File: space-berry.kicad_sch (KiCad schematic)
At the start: 0 parts

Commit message: Stuff
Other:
- sheet PS_PWR renamed ZYNQ_PWR
- sheet PWR_template renamed PWR_3V3
- sheet PWR_template1 renamed PWR_3V3_AUX
- sheet PWR_template2 renamed PWR_1V8
- sheet PWR_template3 renamed PWR_1V2
- sheet PWR_template4 renamed PWR_0V85
- sheet PWR_template5 renamed PWR_5V0
- added sheet PS_DDR_MIO0-53 (PS_DDR_MIO0-53.kicad_sch)
- sheet PWR_0V85: file PWR_template.kicad_sch -> PWR_0V85.kicad_sch
- sheet PWR_1V2: file PWR_template.kicad_sch -> PWR_1V2.kicad_sch
- sheet PWR_1V8: file PWR_template.kicad_sch -> PWR_1V8.kicad_sch
- sheet PWR_3V3: file PWR_template.kicad_sch -> PWR_3V3.kicad_sch
- sheet PWR_3V3_AUX: file PWR_template.kicad_sch -> PWR_3V3_AUX.kicad_sch
- sheet PWR_5V0: file PWR_template.kicad_sch -> PWR_5V0.kicad_sch
- sheet ZYNQ_PWR: file PS_PWR.kicad_sch -> ZYNQ_PWR.kicad_sch
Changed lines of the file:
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@@
     (stroke (width 0.1524) (type solid))
     (fill (color 0 0 0 0.0000))
-    (property "Sheetname" "PS_PWR" (at 76.2 88.1884 0)
+    (property "Sheetname" "ZYNQ_PWR" (at 76.2 88.1884 0)
       (effects (font (size 1.27 1.27)) (justify left bottom))
     )
-    (property "Sheetfile" "PS_PWR.kicad_sch" (at 76.2 102.1846 0)
+    (property "Sheetfile" "ZYNQ_PWR.kicad_sch" (at 76.2 102.1846 0)
       (effects (font (size 1.27 1.27)) (justify left top))
     )
@@
     (stroke (width 0.1524) (type solid))
     (fill (color 0 0 0 0.0000))
-    (property "Sheetname" "PWR_template" (at 38.1 37.3884 0)
+    (property "Sheetname" "PWR_3V3" (at 38.1 37.3884 0)
       (effects (font (size 1.27 1.27)) (justify left bottom))
     )
-    (property "Sheetfile" "PWR_template.kicad_sch" (at 38.1 51.3846 0)
+    (property "Sheetfile" "PWR_3V3.kicad_sch" (at 38.1 51.3846 0)
       (effects (font (size 1.27 1.27)) (justify left top))
     )
@@
     (stroke (width 0.1524) (type solid))
     (fill (color 0 0 0 0.0000))
-    (property "Sheetname" "PWR_template3" (at 38.1 113.5884 0)
+    (property "Sheetname" "PWR_1V2" (at 38.1 113.5884 0)
       (effects (font (size 1.27 1.27)) (justify left bottom))
     )
-    (property "Sheetfile" "PWR_template.kicad_sch" (at 38.1 127.5846 0)
+    (property "Sheetfile" "PWR_1V2.kicad_sch" (at 38.1 127.5846 0)
       (effects (font (size 1.27 1.27)) (justify left top))
     )
@@
     )
   )
+  (sheet (at 152.4 63.5) (size 25.4 12.7) (fields_autoplaced)
+    (stroke (width 0.1524) (type solid))
+    (fill (color 0 0 0 0.0000))
+    (property "Sheetname" "PS_DDR_MIO0-53" (at 152.4 62.7884 0)
+      (effects (font (size 1.27 1.27)) (justify left bottom))
+    )
+    (property "Sheetfile" "PS_DDR_MIO0-53.kicad_sch" (at 152.4 76.7846 0)
+      (effects (font (size 1.27 1.27)) (justify left top))
+    )
+    (instances
+      (project "space-berry"
+        (path "/93269f17-932e-47e4-8e03-ce157f57b85f" (page "16"))
+      )
+    )
+  )
   (sheet (at 38.1 165.1) (size 25.4 12.7) (fields_autoplaced)
     (stroke (width 0.1524) (type solid))
     (fill (color 0 0 0 0.0000))
-    (property "Sheetname" "PWR_template5" (at 38.1 164.3884 0)
+    (property "Sheetname" "PWR_5V0" (at 38.1 164.3884 0)
       (effects (font (size 1.27 1.27)) (justify left bottom))
     )
-    (property "Sheetfile" "PWR_template.kicad_sch" (at 38.1 178.3846 0)
+    (property "Sheetfile" "PWR_5V0.kicad_sch" (at 38.1 178.3846 0)
       (effects (font (size 1.27 1.27)) (justify left top))
     )
@@
     (stroke (width 0.1524) (type solid))
     (fill (color 0 0 0 0.0000))
-    (property "Sheetname" "PWR_template1" (at 38.1 62.7884 0)
+    (property "Sheetname" "PWR_3V3_AUX" (at 38.1 62.7884 0)
       (effects (font (size 1.27 1.27)) (justify left bottom))
     )
-    (property "Sheetfile" "PWR_template.kicad_sch" (at 38.1 76.7846 0)
+    (property "Sheetfile" "PWR_3V3_AUX.kicad_sch" (at 38.1 76.7846 0)
       (effects (font (size 1.27 1.27)) (justify left top))
     )
@@
     (stroke (width 0.1524) (type solid))
     (fill (color 0 0 0 0.0000))
-    (property "Sheetname" "PWR_template4" (at 38.1 138.9884 0)
+    (property "Sheetname" "PWR_0V85" (at 38.1 138.9884 0)
       (effects (font (size 1.27 1.27)) (justify left bottom))
     )
-    (property "Sheetfile" "PWR_template.kicad_sch" (at 38.1 152.9846 0)
+    (property "Sheetfile" "PWR_0V85.kicad_sch" (at 38.1 152.9846 0)
       (effects (font (size 1.27 1.27)) (justify left top))
     )
@@
     (stroke (width 0.1524) (type solid))
     (fill (color 0 0 0 0.0000))
-    (property "Sheetname" "PWR_template2" (at 38.1 88.1884 0)
+    (property "Sheetname" "PWR_1V8" (at 38.1 88.1884 0)
       (effects (font (size 1.27 1.27)) (justify left bottom))
     )
-    (property "Sheetfile" "PWR_template.kicad_sch" (at 38.1 102.1846 0)
+    (property "Sheetfile" "PWR_1V8.kicad_sch" (at 38.1 102.1846 0)
       (effects (font (size 1.27 1.27)) (justify left top))
     )

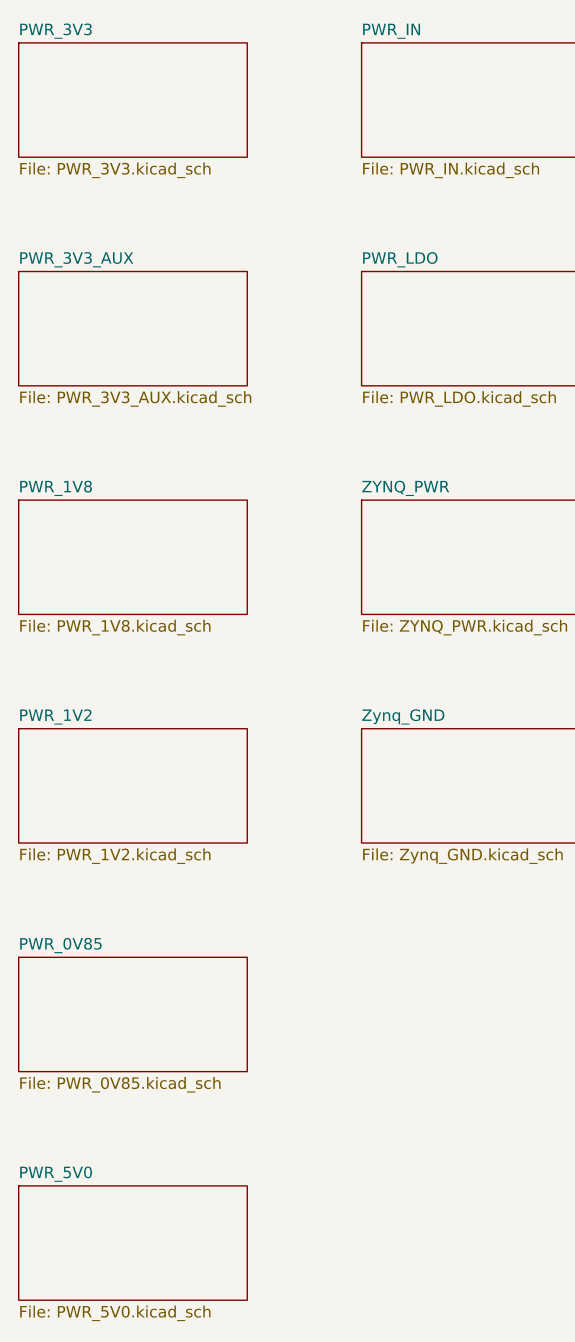
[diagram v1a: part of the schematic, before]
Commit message: DDR4 data lines
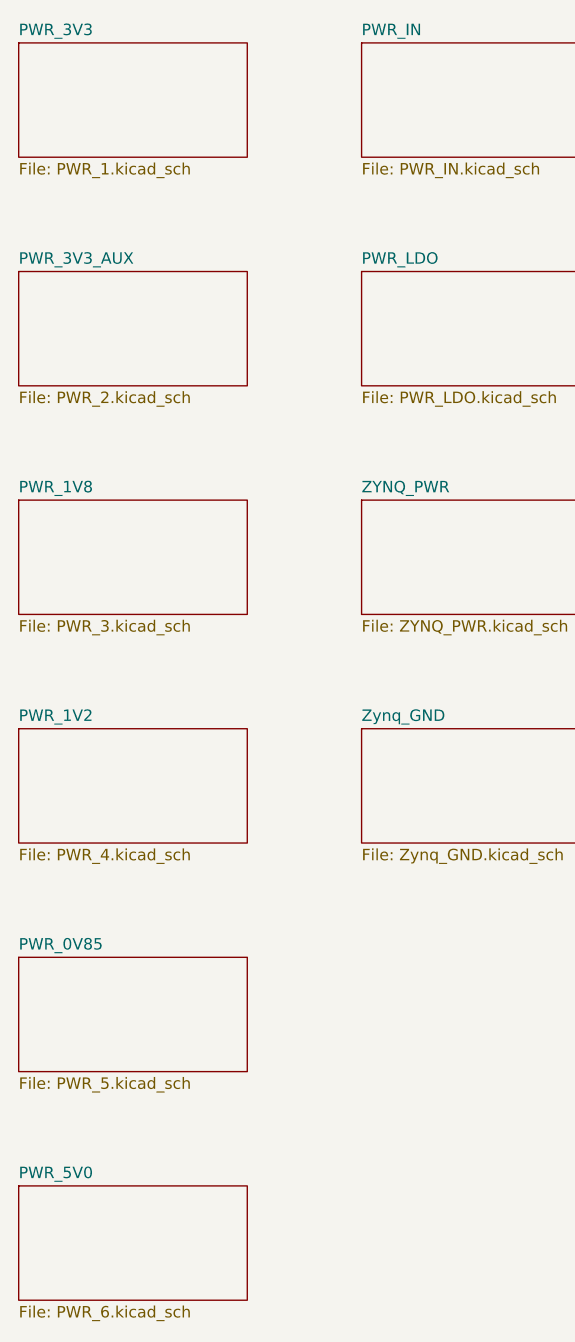
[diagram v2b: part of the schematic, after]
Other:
- sheet PWR_0V85: file PWR_0V85.kicad_sch -> PWR_5.kicad_sch
- sheet PWR_1V2: file PWR_1V2.kicad_sch -> PWR_4.kicad_sch
- sheet PWR_1V8: file PWR_1V8.kicad_sch -> PWR_3.kicad_sch
- sheet PWR_3V3: file PWR_3V3.kicad_sch -> PWR_1.kicad_sch
- sheet PWR_3V3_AUX: file PWR_3V3_AUX.kicad_sch -> PWR_2.kicad_sch
- sheet PWR_5V0: file PWR_5V0.kicad_sch -> PWR_6.kicad_sch
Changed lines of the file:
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@@
       (effects (font (size 1.27 1.27)) (justify left bottom))
     )
-    (property "Sheetfile" "PWR_3V3.kicad_sch" (at 38.1 51.3846 0)
+    (property "Sheetfile" "PWR_1.kicad_sch" (at 38.1 51.3846 0)
       (effects (font (size 1.27 1.27)) (justify left top))
     )
@@
       (effects (font (size 1.27 1.27)) (justify left bottom))
     )
-    (property "Sheetfile" "PWR_1V2.kicad_sch" (at 38.1 127.5846 0)
+    (property "Sheetfile" "PWR_4.kicad_sch" (at 38.1 127.5846 0)
       (effects (font (size 1.27 1.27)) (justify left top))
     )
@@
       (effects (font (size 1.27 1.27)) (justify left bottom))
     )
-    (property "Sheetfile" "PWR_5V0.kicad_sch" (at 38.1 178.3846 0)
+    (property "Sheetfile" "PWR_6.kicad_sch" (at 38.1 178.3846 0)
       (effects (font (size 1.27 1.27)) (justify left top))
     )
@@
       (effects (font (size 1.27 1.27)) (justify left bottom))
     )
-    (property "Sheetfile" "PWR_3V3_AUX.kicad_sch" (at 38.1 76.7846 0)
+    (property "Sheetfile" "PWR_2.kicad_sch" (at 38.1 76.7846 0)
       (effects (font (size 1.27 1.27)) (justify left top))
+    )
+    (property "Field2" "" (at 38.1 63.5 0)
+      (effects (font (size 1.27 1.27)) hide)
     )
     (instances
@@
       (effects (font (size 1.27 1.27)) (justify left bottom))
     )
-    (property "Sheetfile" "PWR_0V85.kicad_sch" (at 38.1 152.9846 0)
+    (property "Sheetfile" "PWR_5.kicad_sch" (at 38.1 152.9846 0)
       (effects (font (size 1.27 1.27)) (justify left top))
     )
@@
       (effects (font (size 1.27 1.27)) (justify left bottom))
     )
-    (property "Sheetfile" "PWR_1V8.kicad_sch" (at 38.1 102.1846 0)
+    (property "Sheetfile" "PWR_3.kicad_sch" (at 38.1 102.1846 0)
       (effects (font (size 1.27 1.27)) (justify left top))
     )
+    (property "Field2" "" (at 38.1 88.9 0)
+      (effects (font (size 1.27 1.27)) hide)
+    )
     (instances

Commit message: DDR4 finish
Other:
- sheet PWR_1V2: file PWR_4.kicad_sch -> PWR_3.kicad_sch
- sheet PWR_1V8: file PWR_3.kicad_sch -> PWR_4.kicad_sch
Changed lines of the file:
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@@
     (stroke (width 0.1524) (type solid))
     (fill (color 0 0 0 0.0000))
-    (property "Sheetname" "PWR_1V2" (at 38.1 113.5884 0)
+    (property "Sheetname" "PWR_1V8" (at 38.1 113.5884 0)
       (effects (font (size 1.27 1.27)) (justify left bottom))
     )
@@
     (stroke (width 0.1524) (type solid))
     (fill (color 0 0 0 0.0000))
-    (property "Sheetname" "PWR_1V8" (at 38.1 88.1884 0)
+    (property "Sheetname" "PWR_1V2" (at 38.1 88.1884 0)
       (effects (font (size 1.27 1.27)) (justify left bottom))
     )

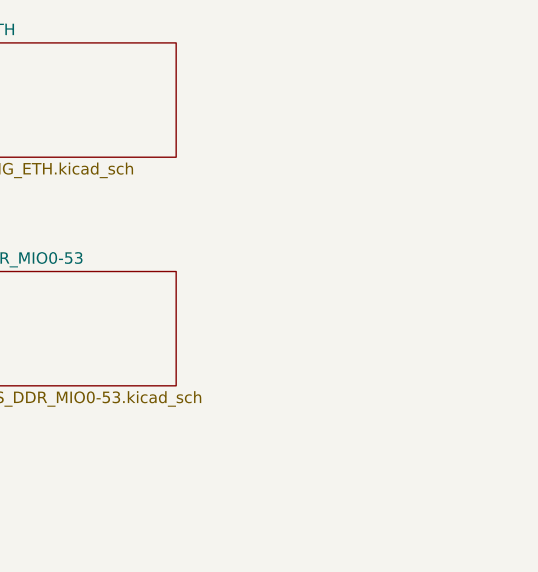
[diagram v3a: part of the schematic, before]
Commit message: Gbe routing
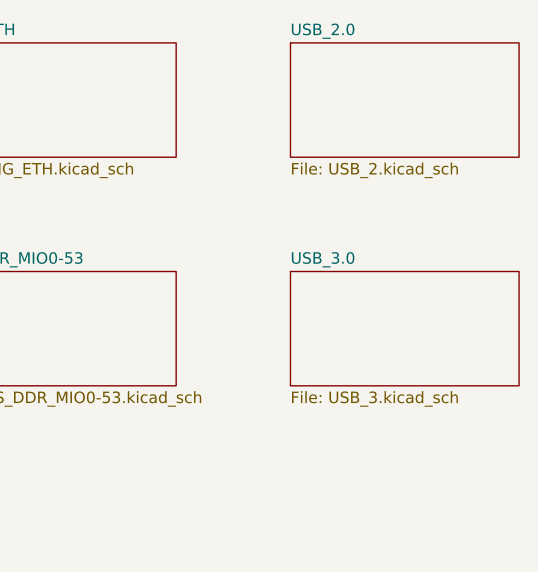
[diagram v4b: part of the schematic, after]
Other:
- added sheet USB_2.0 (USB_2.kicad_sch)
- added sheet USB_3.0 (USB_3.kicad_sch)
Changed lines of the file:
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@@
+    )
+  )
+  (sheet (at 190.5 63.5) (size 25.4 12.7) (fields_autoplaced)
+    (stroke (width 0.1524) (type solid))
+    (fill (color 0 0 0 0.0000))
+    (property "Sheetname" "USB_3.0" (at 190.5 62.7884 0)
+      (effects (font (size 1.27 1.27)) (justify left bottom))
+    )
+    (property "Sheetfile" "USB_3.kicad_sch" (at 190.5 76.7846 0)
+      (effects (font (size 1.27 1.27)) (justify left top))
+    )
+    (instances
+      (project "space-berry"
+        (path "/93269f17-932e-47e4-8e03-ce157f57b85f" (page "18"))
+      )
+    )
+  )
+  (sheet (at 190.5 38.1) (size 25.4 12.7) (fields_autoplaced)
+    (stroke (width 0.1524) (type solid))
+    (fill (color 0 0 0 0.0000))
+    (property "Sheetname" "USB_2.0" (at 190.5 37.3884 0)
+      (effects (font (size 1.27 1.27)) (justify left bottom))
+    )
+    (property "Sheetfile" "USB_2.kicad_sch" (at 190.5 51.3846 0)
+      (effects (font (size 1.27 1.27)) (justify left top))
+    )
+    (property "Field2" "" (at 190.5 38.1 0)
+      (effects (font (size 1.27 1.27)) hide)
+    )
+    (instances
+      (project "space-berry"
+        (path "/93269f17-932e-47e4-8e03-ce157f57b85f" (page "17"))
+      )
     )
   )

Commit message: usb and stuff
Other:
- removed sheet USB_3.0
- added sheet GiTx (GiTx.kicad_sch)
- added sheet PLL (PLL.kicad_sch)
- added sheet USB_2_2 (USB_2_2.kicad_sch)

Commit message: a.
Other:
- sheet USB_2.0 renamed USB_0
- sheet USB_2_2 renamed USB_1
- added sheet pcie (pcie.kicad_sch)
- added sheet sata (sata.kicad_sch)
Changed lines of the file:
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@@
+    )
+  )
+  (sheet (at 190.5 88.9) (size 25.4 12.7) (fields_autoplaced)
+    (stroke (width 0.1524) (type solid))
+    (fill (color 0 0 0 0.0000))
+    (property "Sheetname" "pcie" (at 190.5 88.1884 0)
+      (effects (font (size 1.27 1.27)) (justify left bottom))
+    )
+    (property "Sheetfile" "pcie.kicad_sch" (at 190.5 102.1846 0)
+      (effects (font (size 1.27 1.27)) (justify left top))
+    )
+    (property "Field2" "" (at 190.5 88.9 0)
+      (effects (font (size 1.27 1.27)) hide)
+    )
+    (instances
+      (project "space-berry"
+        (path "/93269f17-932e-47e4-8e03-ce157f57b85f" (page "21"))
+      )
     )
   )
@@
     (stroke (width 0.1524) (type solid))
     (fill (color 0 0 0 0.0000))
-    (property "Sheetname" "USB_2.0" (at 190.5 37.3884 0)
+    (property "Sheetname" "USB_0" (at 190.5 37.3884 0)
       (effects (font (size 1.27 1.27)) (justify left bottom))
     )
@@
       (project "space-berry"
         (path "/93269f17-932e-47e4-8e03-ce157f57b85f" (page "17"))
+      )
+    )
+  )
+  (sheet (at 190.5 114.3) (size 25.4 12.7) (fields_autoplaced)
+    (stroke (width 0.1524) (type solid))
+    (fill (color 0 0 0 0.0000))
+    (property "Sheetname" "sata" (at 190.5 113.5884 0)
+      (effects (font (size 1.27 1.27)) (justify left bottom))
+    )
+    (property "Sheetfile" "sata.kicad_sch" (at 190.5 127.5846 0)
+      (effects (font (size 1.27 1.27)) (justify left top))
+    )
+    (property "Field2" "" (at 190.5 114.3 0)
+      (effects (font (size 1.27 1.27)) hide)
+    )
+    (instances
+      (project "space-berry"
+        (path "/93269f17-932e-47e4-8e03-ce157f57b85f" (page "22"))
       )
     )
@@
     (stroke (width 0.1524) (type solid))
     (fill (color 0 0 0 0.0000))
-    (property "Sheetname" "USB_2_2" (at 190.5 62.7884 0)
+    (property "Sheetname" "USB_1" (at 190.5 62.7884 0)
       (effects (font (size 1.27 1.27)) (justify left bottom))
     )
